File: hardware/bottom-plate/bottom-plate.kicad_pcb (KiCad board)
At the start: 2 copper layers, 77.2 x 77.2 mm, 5 parts

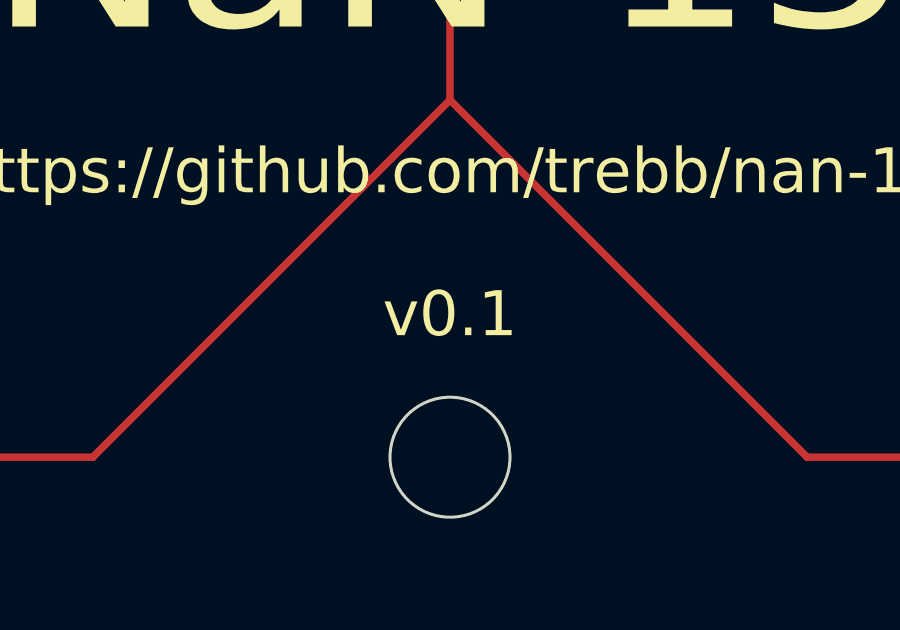
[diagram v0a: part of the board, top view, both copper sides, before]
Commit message: Update version numbers on PCB silkscreens
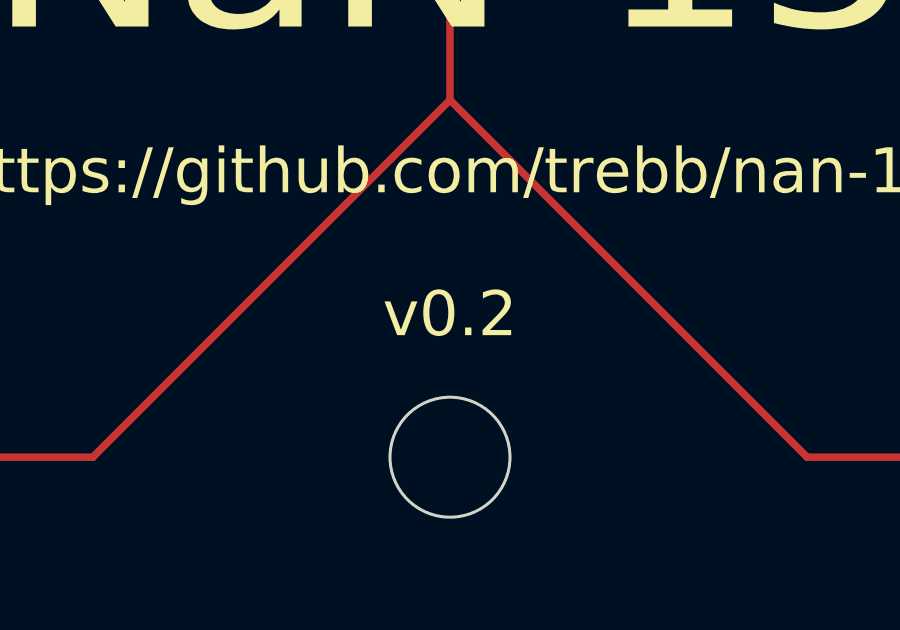
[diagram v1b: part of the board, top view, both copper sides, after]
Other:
- board text added: "v0.2"
- board text removed: "v0.1"
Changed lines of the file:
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@@
   (page A4)
   (layers
-    (0 F.Cu signal)
+    (0 F.Cu signal hide)
     (31 B.Cu signal hide)
     (32 B.Adhes user)
@@
       (xy 0.500964 3.601424)) (layer B.SilkS) (width 0.01))
   )
-  (gr_text v0.1 (at 150.01875 126.20625) (layer F.SilkS)
+  (gr_text v0.2 (at 150.01875 126.20625) (layer F.SilkS)
     (effects (font (size 1.5 1.5) (thickness 0.3)))
   )

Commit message: Various PCB edits
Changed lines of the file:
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@@
   )
   (page A4)
+  (title_block
+    (title NaN-15)
+    (rev 0.2)
+    (comment 1 "Bottom plate")
+  )
   (layers
-    (0 F.Cu signal hide)
-    (31 B.Cu signal hide)
+    (0 F.Cu signal)
+    (31 B.Cu signal)
     (32 B.Adhes user)
     (33 F.Adhes user)
@@
       (xy 0.500964 3.601424)) (layer B.SilkS) (width 0.01))
   )
-  (gr_text v0.2 (at 150.01875 126.20625) (layer F.SilkS)
+  (gr_text v0.2 (at 119.0625 123.825) (layer F.SilkS)
     (effects (font (size 1.5 1.5) (thickness 0.3)))
   )
@@
     (effects (font (size 1.5 1.5) (thickness 0.3)) (justify mirror))
   )
-  (gr_text https://github.com/trebb/nan-15 (at 150.01875 121.44375) (layer F.SilkS)
+  (gr_text https://github.com/trebb/nan-15 (at 150.01875 123.825) (layer F.SilkS)
     (effects (font (size 1.5 1.5) (thickness 0.3)))
   )
-  (gr_text NaN-15 (at 150.01875 114.3) (layer F.SilkS)
+  (gr_text NaN-15 (at 150.01875 119.0625) (layer F.SilkS)
     (effects (font (size 5 6) (thickness 0.6)))
   )
